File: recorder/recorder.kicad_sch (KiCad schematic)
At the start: 2 parts, among them U1 IM73D122V01, U2 ADAU7118

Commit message: schematics start
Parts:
- added J1: Conn_02x03_Odd_Even, symbol recorder:JETSON_CONNECTOR
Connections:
- net DAT0: now reaches U1.1 (DATA)
- net +3.3V: now reaches U1.2 (VDD)
- net +3.3V: now also U1.4 (LR), J1.1 (Vcc)
- net CLK0: now reaches U1.3 (CLOCK)
- net GND: now reaches U1.5 (GND)
- net GND: now also J1.2 (GND)
- new net I2S1: J1.3 (I2S1)

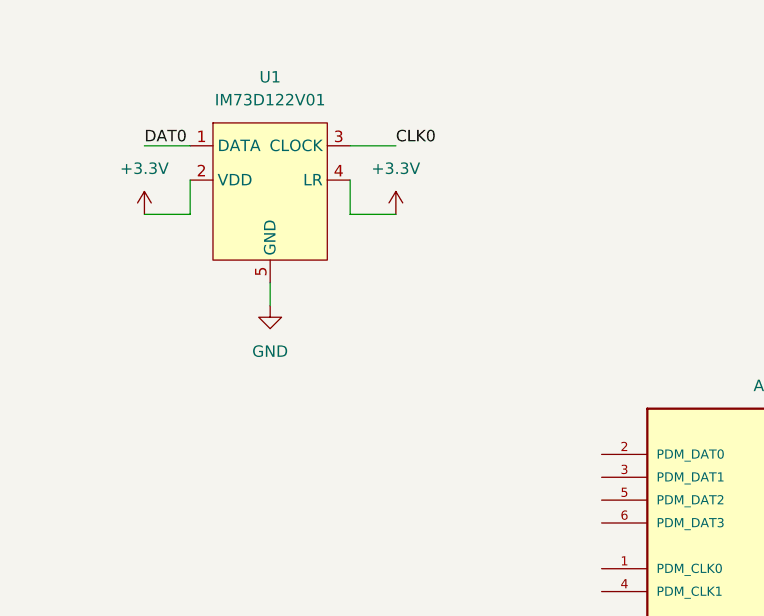
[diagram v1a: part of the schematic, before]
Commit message: hierarchal structures
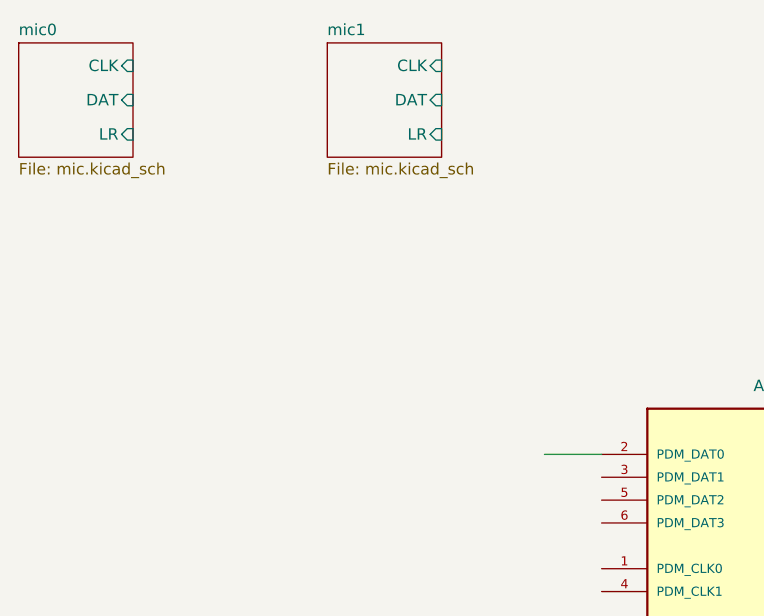
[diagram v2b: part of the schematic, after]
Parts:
- removed U1: IM73D122V01, Library:IM73D122V01, symbol recorder:IM73D122V01
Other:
- added sheet mic0 (mic.kicad_sch)
- added sheet mic1 (mic.kicad_sch)

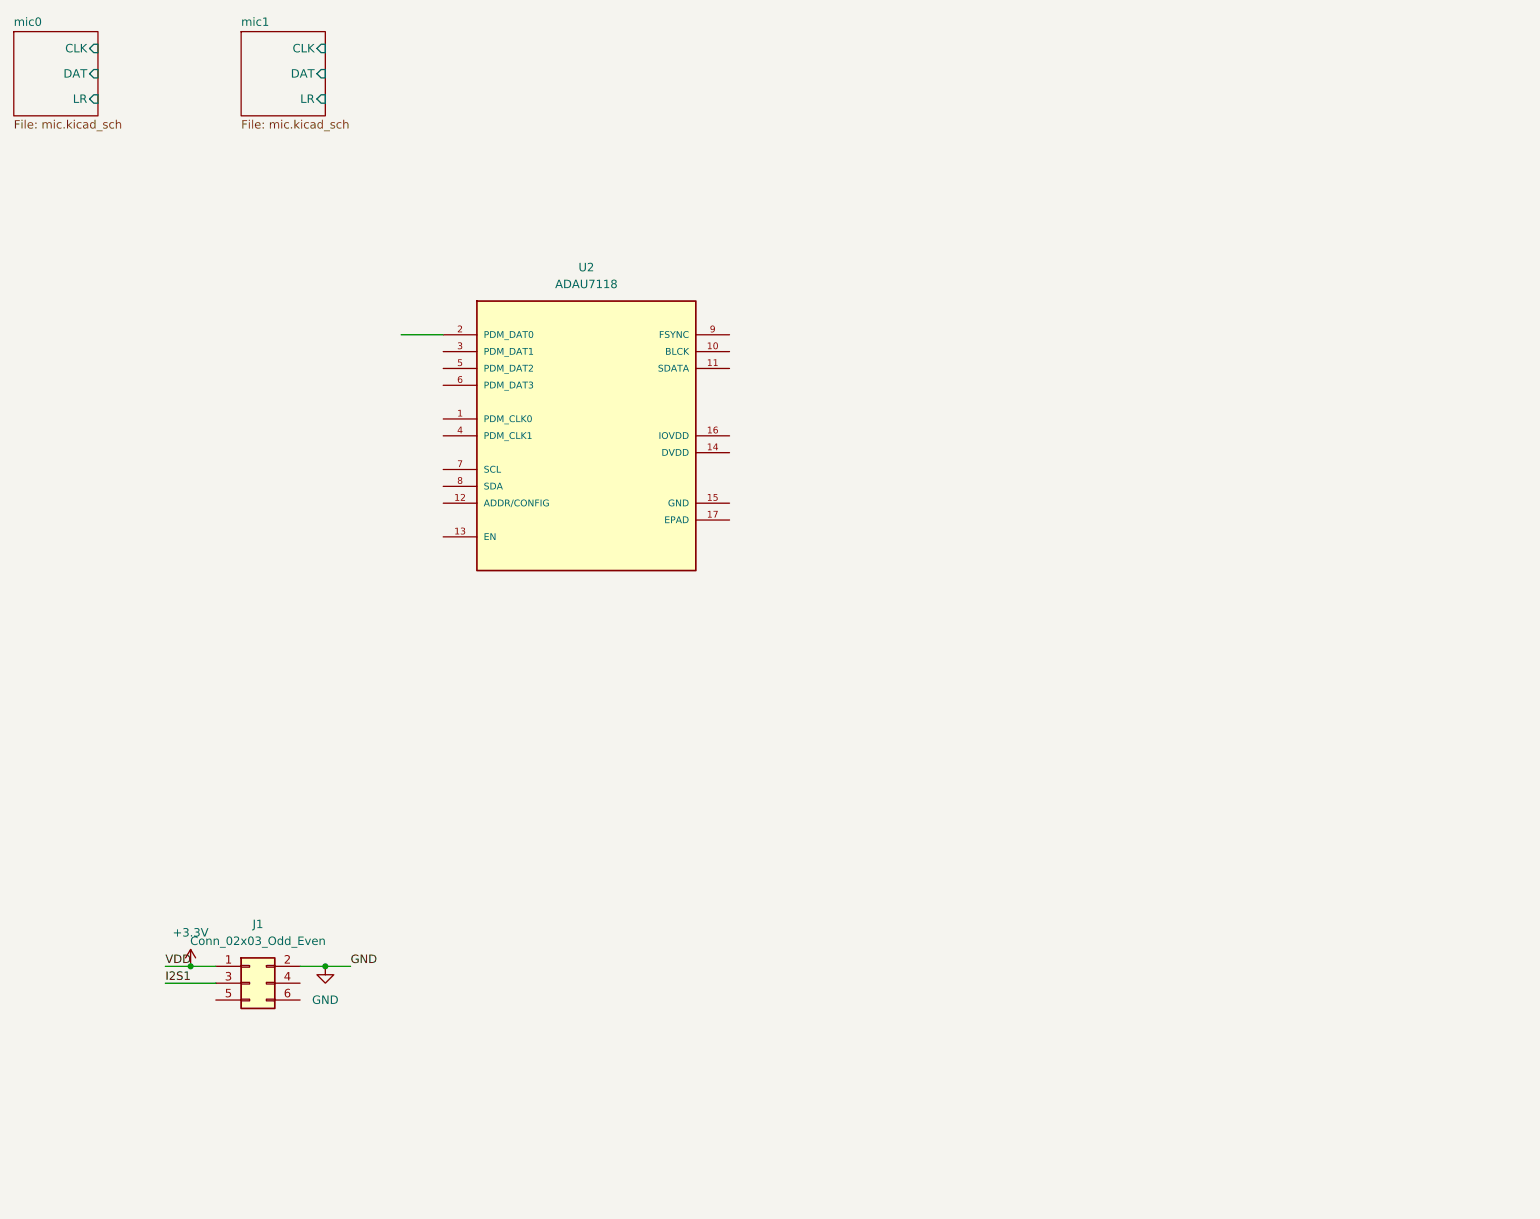
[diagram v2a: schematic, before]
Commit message: added LDO
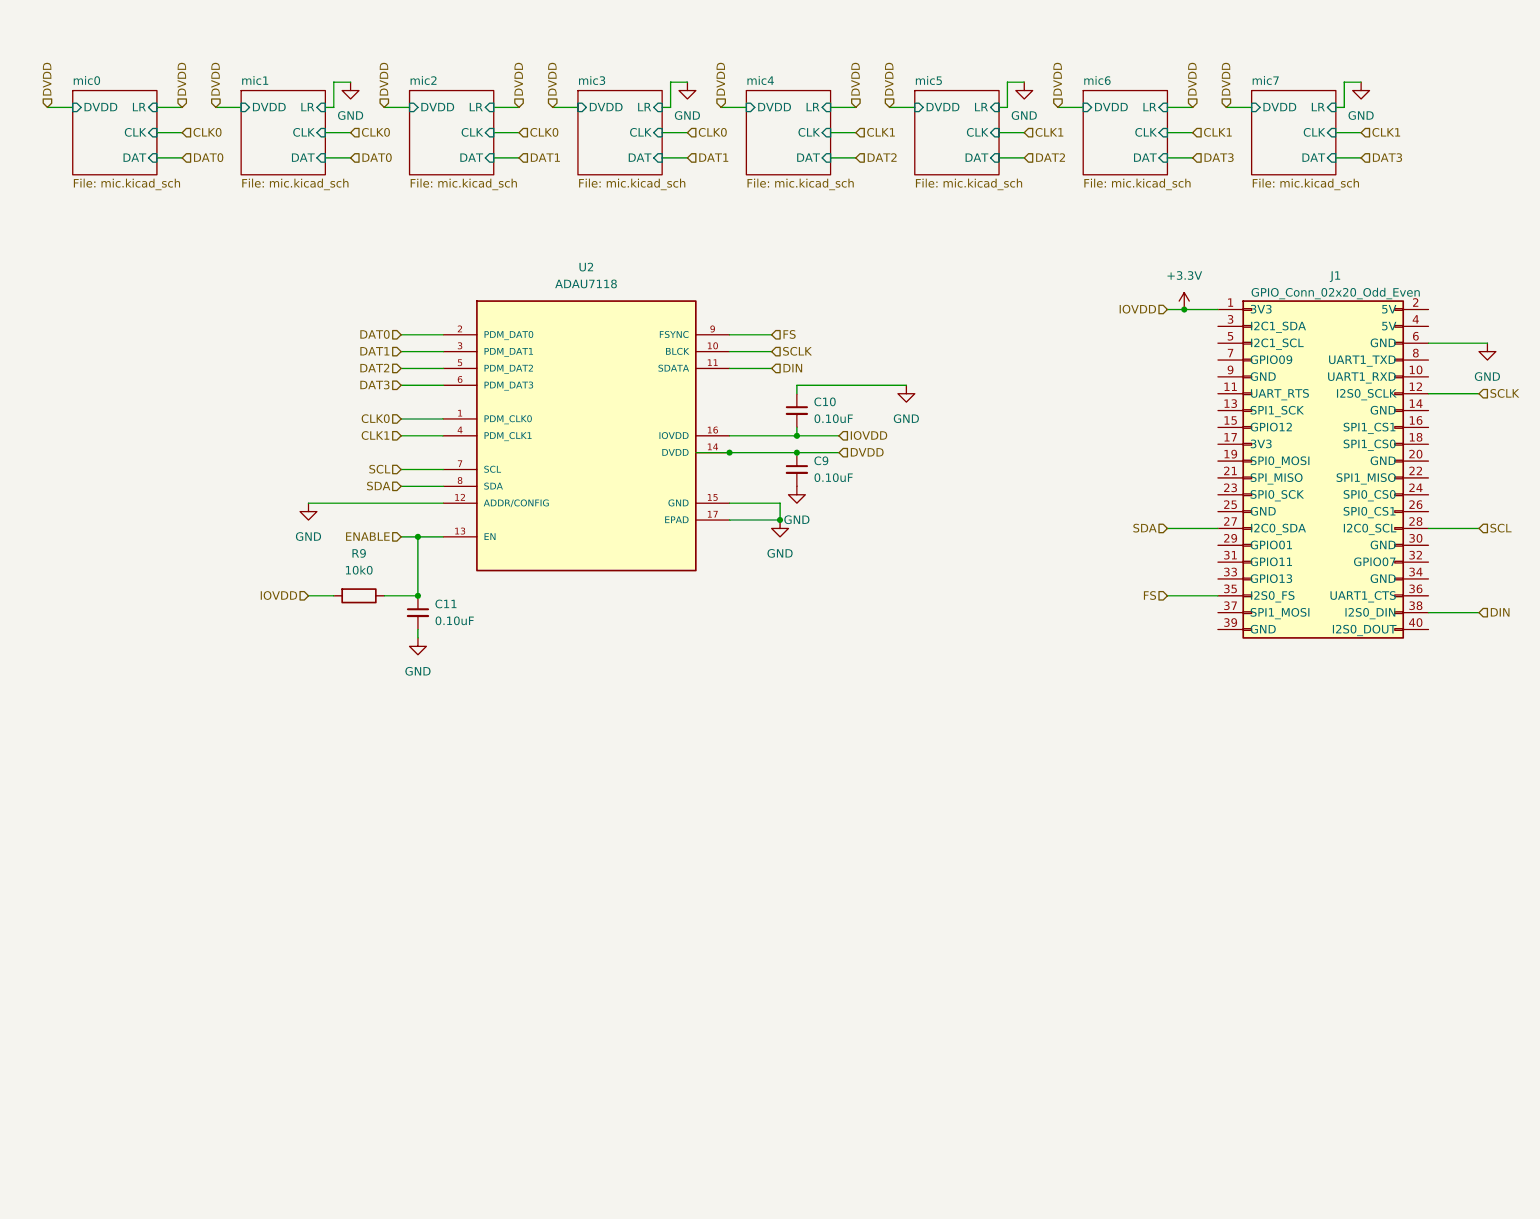
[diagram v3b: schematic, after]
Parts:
- removed J1: Conn_02x03_Odd_Even, symbol recorder:JETSON_CONNECTOR
- added C10, C11, C9: 0.10uF, symbol recorder:C_Small_1
- added J1: GPIO_Conn_02x20_Odd_Even, symbol recorder:GPIO_Conn_02x20_Odd_Even
- added R9: 10k0, symbol Device:R
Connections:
- net +3.3V: now also U2.16 (IOVDD), C10.2, J1.1 (3V3), R9.2
- net GND: now also U2.12 (ADDR/CONFIG), U2.15 (GND), U2.17 (EPAD), C10.1, C11.2, C9.2, J1.6 (GND)
- net CLK0: now reaches U2.1 (PDM_CLK0)
- net SCLK: now reaches U2.10 (BLCK)
- net SCLK: now also J1.12 (I2S0_SCLK)
- net DIN: now reaches U2.11 (SDATA)
- net DIN: now also J1.38 (I2S0_DIN)
- net ENABLE: now reaches U2.13 (EN)
- net ENABLE: now also C11.1, R9.1
- net DVDD: now reaches U2.14 (DVDD)
- net DVDD: now also C9.1
- net DAT0: now reaches U2.2 (PDM_DAT0)
- net DAT1: now reaches U2.3 (PDM_DAT1)
- net CLK1: now reaches U2.4 (PDM_CLK1)
- net DAT2: now reaches U2.5 (PDM_DAT2)
- net DAT3: now reaches U2.6 (PDM_DAT3)
- net SCL: now reaches U2.7 (SCL)
- net SCL: now also J1.28 (I2C0_SCL)
- net SDA: now reaches U2.8 (SDA)
- net SDA: now also J1.27 (I2C0_SDA)
- net FS: now reaches U2.9 (FSYNC)
- net FS: now also J1.35 (I2S0_FS)
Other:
- added sheet mic2 (mic.kicad_sch)
- added sheet mic3 (mic.kicad_sch)
- added sheet mic4 (mic.kicad_sch)
- added sheet mic5 (mic.kicad_sch)
- added sheet mic6 (mic.kicad_sch)
- added sheet mic7 (mic.kicad_sch)
- sheet mic0 ports: added DVDD; removed none
- sheet mic1 ports: added DVDD; removed none

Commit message: fixing capacitor footprints
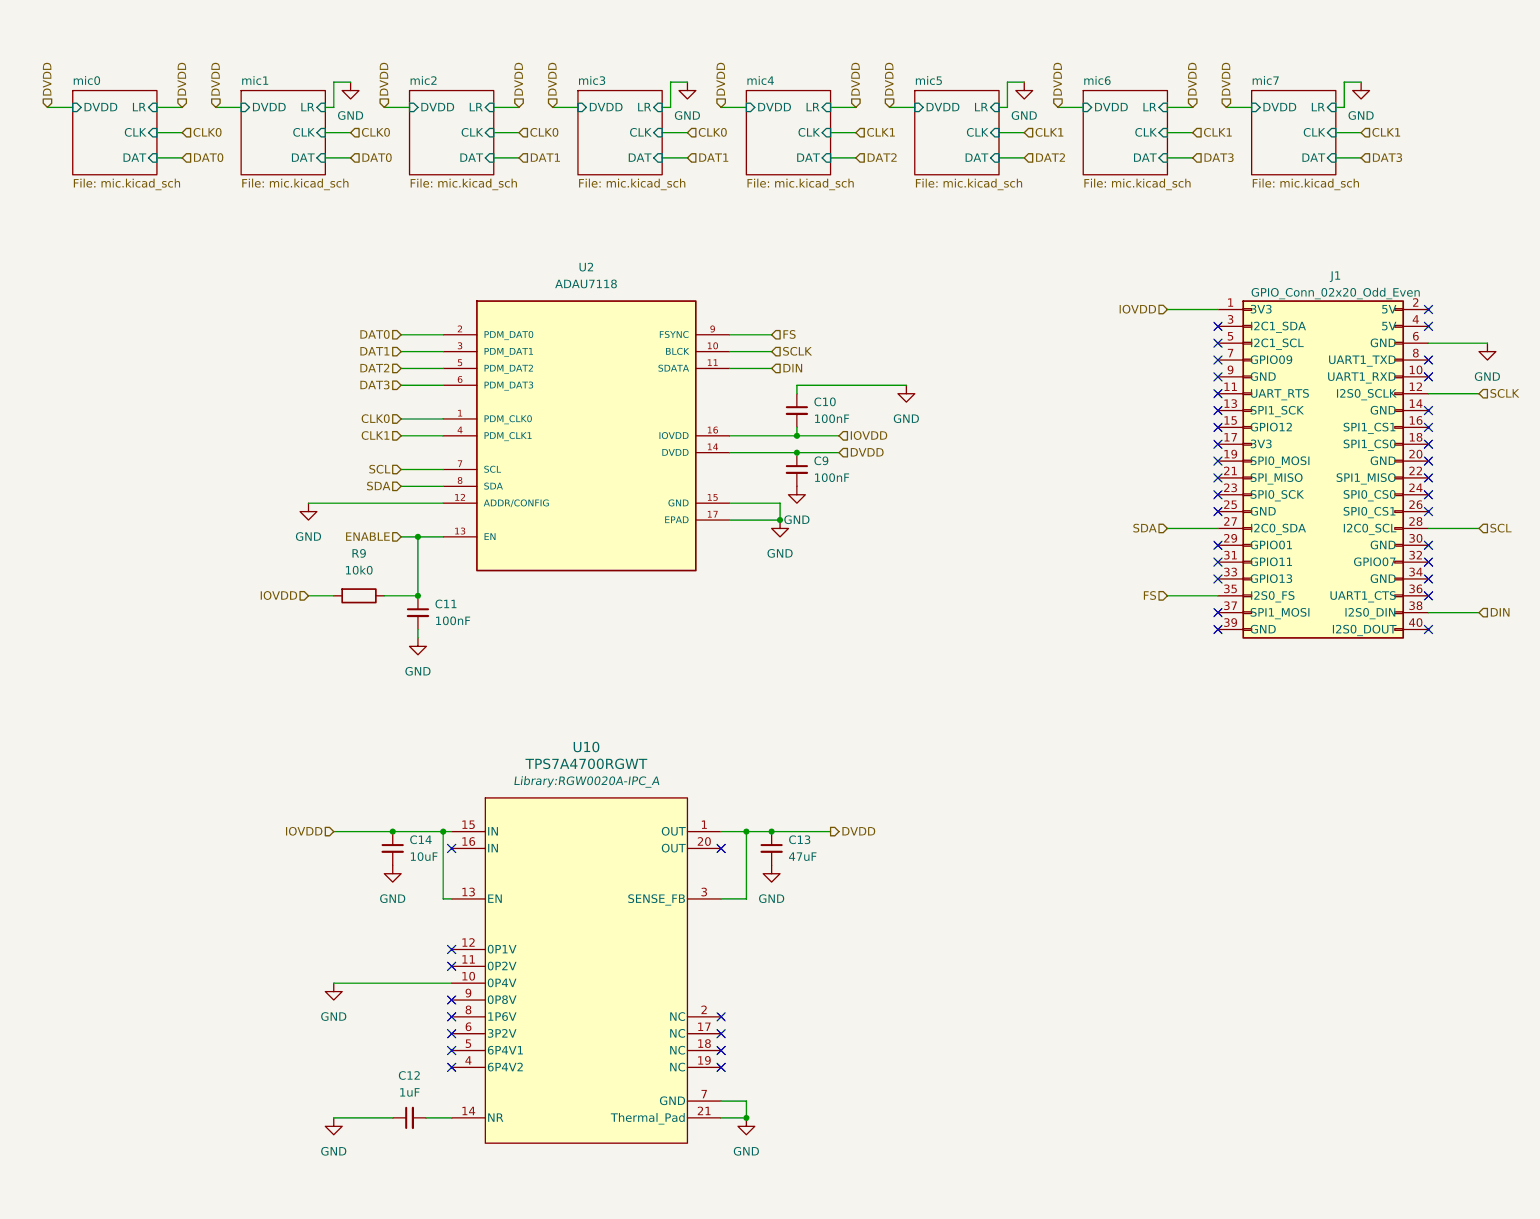
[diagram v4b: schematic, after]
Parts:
- added C12: 1uF, symbol recorder:C_Small_1
- added C13: 47uF, symbol recorder:C_Small_1
- added C14: 10uF, symbol recorder:C_Small_1
- added U10: TPS7A4700RGWT, Library:RGW0020A-IPC_A, symbol recorder:TPS7A4700RGWT
- C10, C11, C9: value 0.10uF -> 100nF
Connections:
- net DVDD: now also C13.1, U10.1 (OUT), U10.3 (SENSE_FB)
- net GND: now also C12.1, C13.2, C14.2, U10.10 (0P4V), U10.21 (Thermal_Pad), U10.7 (GND)
- net +3.3V renamed IOVDD
- net IOVDD: now also C14.1, U10.13 (EN), U10.15 (IN)
- new net: C12.2, U10.14 (NR)
- no-connect marks 0 -> 46

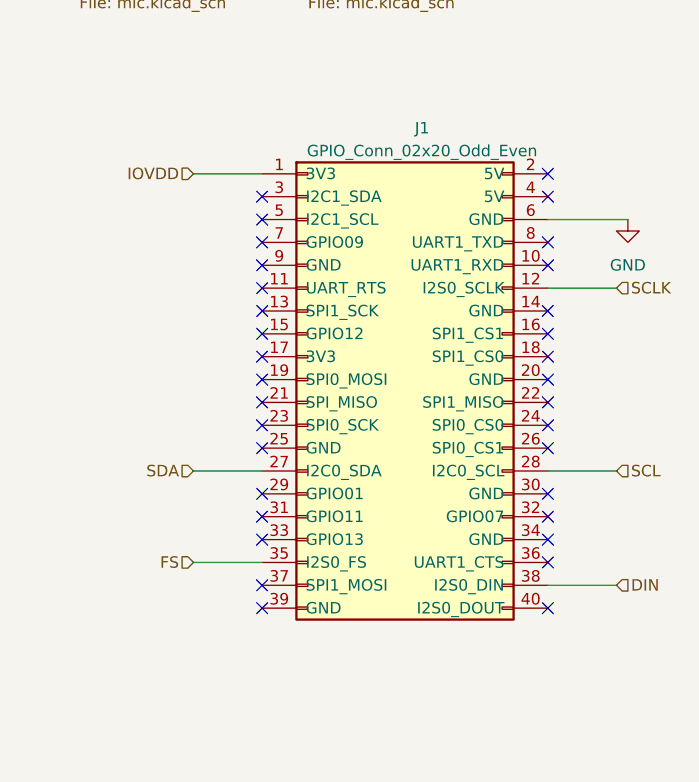
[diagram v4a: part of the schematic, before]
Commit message: spaced out microphones
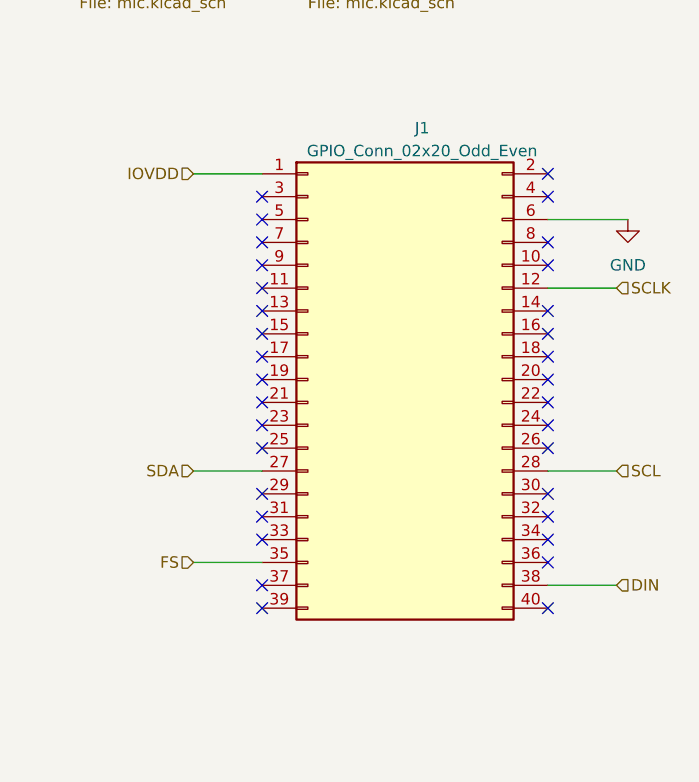
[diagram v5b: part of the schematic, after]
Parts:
- C10, C11, C12, C13, C14, C9: footprint (none) -> Library:C_0603_1608Metric
- J1: footprint (none) -> Library:PinHeader_2x20_P2.54mm_Vertical
- R9: footprint (none) -> Library:R_0603_1608Metric
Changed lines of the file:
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@@
 			)
 		)
-		(property "Footprint" ""
+		(property "Footprint" "Library:C_0603_1608Metric"
 			(at 77.47 104.14 0)
 			(effects
@@
 			)
 		)
-		(property "Footprint" ""
+		(property "Footprint" "Library:PinHeader_2x20_P2.54mm_Vertical"
 			(at 214.63 82.55 0)
 			(effects
@@
 			)
 		)
-		(property "Footprint" ""
+		(property "Footprint" "Library:R_0603_1608Metric"
 			(at 68.58 99.822 90)
 			(effects
@@
 			)
 		)
-		(property "Footprint" ""
+		(property "Footprint" "Library:C_0603_1608Metric"
 			(at 130.81 139.7 0)
 			(effects
@@
 			)
 		)
-		(property "Footprint" ""
+		(property "Footprint" "Library:C_0603_1608Metric"
 			(at 134.62 73.66 0)
 			(effects
@@
 			)
 		)
-		(property "Footprint" ""
+		(property "Footprint" "Library:C_0603_1608Metric"
 			(at 134.62 82.55 0)
 			(effects
@@
 			)
 		)
-		(property "Footprint" ""
+		(property "Footprint" "Library:C_0603_1608Metric"
 			(at 73.66 139.7 0)
 			(effects
@@
 			)
 		)
-		(property "Footprint" ""
+		(property "Footprint" "Library:C_0603_1608Metric"
 			(at 76.2 180.34 0)
 			(effects

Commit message: v1
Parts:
- added R10, R11: 2k2, Library:R_0603_1608Metric, symbol Device:R
- added R12, R13: 22, Library:R_0603_1608Metric, symbol Device:R
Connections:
- net CLK0: now also R12.2; no longer U2.1 (PDM_CLK0)
- net CLK1: now also R13.2; no longer U2.4 (PDM_CLK1)
- net IOVDD: now also R10.2, R11.2
- net SCL: now also R10.1
- net SDA: now also R11.1
- new net: R13.1, U2.4 (PDM_CLK1)
- new net: R12.1, U2.1 (PDM_CLK0)
